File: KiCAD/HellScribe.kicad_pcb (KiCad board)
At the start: 2 copper layers, 173.7 x 28.4 mm, 49 parts, among them CON1 +12v, J1 STX-3100-5N, Q1 2N3904, Q10 2N3904, Q2 Q_PMOS_GSD, Q3 Q_PMOS_GSD, Q4 Q_PMOS_GSD, Q5 Q_PMOS_GSD, Q6 Q_PMOS_GSD, Q7 Q_PMOS_GSD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

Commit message: Improved PS filtering, updated version to v1.1
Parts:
- added C7: 10uF, Resistors_SMD:R_1206_HandSoldering, F.Cu at (54.4, 115.6)
- added L1: 10uH, Resistors_SMD:R_0805_HandSoldering, F.Cu at (55.1, 118.4)
- moved C6 1.02 mm to (50.8, 119.4)
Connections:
- C6 pad 2: +12V -> Net-(C6-Pad2)
- CON1 pad 1: +12V -> Net-(C6-Pad2)
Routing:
- net Net-(C6-Pad2): track 0.00 -> 6.82 mm
- net +12V: track 36.9 -> 32.7 mm, vias 14 -> 15
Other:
- board text added: "HellScribe v1.1"
- board text removed: "HellScribe v1.0"
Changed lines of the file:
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@@
 (kicad_pcb (version 4) (host pcbnew 4.0.2-stable)
   (general
-    (links 90)
+    (links 93)
     (no_connects 0)
-    (area 31.75 96.52 208.280001 128.270001)
+    (area 32.944999 97.968999 206.831001 126.567001)
     (thickness 1.6)
     (drawings 9)
-    (tracks 350)
+    (tracks 355)
     (zones 0)
-    (modules 49)
-    (nets 41)
+    (modules 51)
+    (nets 42)
   )
   (page A4)
@@
   )
   (setup
-    (last_trace_width 0.25)
+    (last_trace_width 0.5)
     (user_trace_width 0.5)
     (trace_clearance 0.2)
@@
   (net 39 "Net-(U2-Pad12)")
   (net 40 "Net-(Q1-Pad3)")
+  (net 41 "Net-(C6-Pad2)")
   (net_class Default "This is the default net class."
     (clearance 0.2)
@@
     (add_net "Net-(C4-Pad2)")
     (add_net "Net-(C5-Pad2)")
+    (add_net "Net-(C6-Pad2)")
     (add_net "Net-(D1-Pad1)")
     (add_net "Net-(D1-Pad2)")
@@
   )
   (module Capacitors_SMD:C_0603_HandSoldering (layer F.Cu)
-    (at 51.816 119.38 90)
+    (at 50.8 119.38 90)
     (descr "Capacitor SMD 0603, hand soldering")
     (tags "capacitor 0603")
     (attr smd)
-    (fp_text reference C6 (at 0 1.778 90) (layer F.SilkS)
+    (fp_text reference C6 (at -3.048 0 90) (layer F.SilkS)
       (effects (font (size 1 1) (thickness 0.15)))
     )
@@
       (net 2 GND))
     (pad 2 smd rect (at 0.95 0 90) (size 1.2 0.75) (layers F.Cu F.Paste F.Mask)
-      (net 8 +12V))
+      (net 41 "Net-(C6-Pad2)"))
     (model Capacitors_SMD.3dshapes/C_0603_HandSoldering.wrl
       (at (xyz 0 0 0))
@@
     (fp_line (start 7.00024 -4.50088) (end -7.50062 -4.50088) (layer F.SilkS) (width 0.15))
     (pad 1 thru_hole rect (at 6.20014 0) (size 3.50012 3.50012) (drill oval 1.00076 2.99974) (layers *.Cu *.Mask F.SilkS)
-      (net 8 +12V))
+      (net 41 "Net-(C6-Pad2)"))
     (pad 2 thru_hole rect (at 0.20066 0) (size 3.50012 3.50012) (drill oval 1.00076 2.99974) (layers *.Cu *.Mask F.SilkS)
       (net 2 GND))
@@
     )
   )
-  (gr_text "HellScribe v1.0" (at 171.704 104.14) (layer F.SilkS)
+  (module Resistors_SMD:R_1206_HandSoldering (layer F.Cu)
+    (at 54.356 115.57)
+    (descr "Resistor SMD 1206, hand soldering")
+    (tags "resistor 1206")
+    (attr smd)
+    (fp_text reference C7 (at -4.572 0) (layer F.SilkS)
+      (effects (font (size 1 1) (thickness 0.15)))
+    )
+    (fp_text value 10uF (at 0 2.3) (layer F.Fab)
+      (effects (font (size 1 1) (thickness 0.15)))
+    )
+    (fp_line (start -3.3 -1.2) (end 3.3 -1.2) (layer F.CrtYd) (width 0.05))
+    (fp_line (start -3.3 1.2) (end 3.3 1.2) (layer F.CrtYd) (width 0.05))
+    (fp_line (start -3.3 -1.2) (end -3.3 1.2) (layer F.CrtYd) (width 0.05))
+    (fp_line (start 3.3 -1.2) (end 3.3 1.2) (layer F.CrtYd) (width 0.05))
+    (fp_line (start 1 1.075) (end -1 1.075) (layer F.SilkS) (width 0.15))
+    (fp_line (start -1 -1.075) (end 1 -1.075) (layer F.SilkS) (width 0.15))
+    (pad 1 smd rect (at -2 0) (size 2 1.7) (layers F.Cu F.Paste F.Mask)
+      (net 2 GND))
+    (pad 2 smd rect (at 2 0) (size 2 1.7) (layers F.Cu F.Paste F.Mask)
+      (net 8 +12V))
+    (model Resistors_SMD.3dshapes/R_1206_HandSoldering.wrl
+      (at (xyz 0 0 0))
+      (scale (xyz 1 1 1))
+      (rotate (xyz 0 0 0))
+    )
+  )
+  (module Resistors_SMD:R_0805_HandSoldering (layer F.Cu)
+    (at 55.118 118.364 180)
+    (descr "Resistor SMD 0805, hand soldering")
+    (tags "resistor 0805")
+    (attr smd)
+    (fp_text reference L1 (at 0 -2.032 180) (layer F.SilkS)
+      (effects (font (size 1 1) (thickness 0.15)))
+    )
+    (fp_text value 10uH (at 0 2.1 180) (layer F.Fab)
+      (effects (font (size 1 1) (thickness 0.15)))
+    )
+    (fp_line (start -2.4 -1) (end 2.4 -1) (layer F.CrtYd) (width 0.05))
+    (fp_line (start -2.4 1) (end 2.4 1) (layer F.CrtYd) (width 0.05))
+    (fp_line (start -2.4 -1) (end -2.4 1) (layer F.CrtYd) (width 0.05))
+    (fp_line (start 2.4 -1) (end 2.4 1) (layer F.CrtYd) (width 0.05))
+    (fp_line (start 0.6 0.875) (end -0.6 0.875) (layer F.SilkS) (width 0.15))
+    (fp_line (start -0.6 -0.875) (end 0.6 -0.875) (layer F.SilkS) (width 0.15))
+    (pad 1 smd rect (at -1.35 0 180) (size 1.5 1.3) (layers F.Cu F.Paste F.Mask)
+      (net 8 +12V))
+    (pad 2 smd rect (at 1.35 0 180) (size 1.5 1.3) (layers F.Cu F.Paste F.Mask)
+      (net 41 "Net-(C6-Pad2)"))
+    (model Resistors_SMD.3dshapes/R_0805_HandSoldering.wrl
+      (at (xyz 0 0 0))
+      (scale (xyz 1 1 1))
+      (rotate (xyz 0 0 0))
+    )
+  )
+  (gr_text "HellScribe v1.1" (at 171.704 104.14) (layer F.SilkS)
     (effects (font (size 3 3) (thickness 0.5)))
   )
@@
   (segment (start 64.45 103.528) (end 64.6 103.378) (width 0.25) (layer F.Cu) (net 7))
   (segment (start 64.346 105.56) (end 64.45 105.664) (width 0.25) (layer F.Cu) (net 7))
-  (segment (start 51.816 118.43) (end 54.61 118.43) (width 0.5) (layer F.Cu) (net 8))
-  (segment (start 56.558 119.042) (end 55.946 118.43) (width 0.5) (layer F.Cu) (net 8))
-  (segment (start 55.946 118.43) (end 54.61 118.43) (width 0.5) (layer F.Cu) (net 8))
-  (segment (start 56.558 119.042) (end 56.558 122.682) (width 0.5) (layer F.Cu) (net 8))
-  (segment (start 51.816 118.43) (end 47.16014 118.43) (width 0.5) (layer F.Cu) (net 8))
-  (segment (start 47.16014 118.43) (end 47.09414 118.364) (width 0.5) (layer F.Cu) (net 8))
+  (segment (start 56.558 122.682) (end 54.61 122.682) (width 0.5) (layer F.Cu) (net 8))
+  (via (at 54.61 122.682) (size 0.6) (drill 0.4) (layers F.Cu B.Cu) (net 8))
+  (segment (start 56.468 118.364) (end 56.468 122.592) (width 0.5) (layer F.Cu) (net 8))
+  (segment (start 56.468 122.592) (end 56.558 122.682) (width 0.5) (layer F.Cu) (net 8))
+  (segment (start 56.468 118.364) (end 56.468 115.682) (width 0.5) (layer F.Cu) (net 8))
+  (segment (start 56.468 115.682) (end 56.356 115.57) (width 0.5) (layer F.Cu) (net 8))
   (segment (start 55.626 105.58) (end 55.626 103.886) (width 0.5) (layer F.Cu) (net 8))
   (via (at 55.626 103.886) (size 0.6) (drill 0.4) (layers F.Cu B.Cu) (net 8))
@@
   (segment (start 59.055 108.077) (end 58.674 108.458) (width 0.25) (layer F.Cu) (net 40))
   (segment (start 58.758 122.258) (end 58.758 122.682) (width 0.25) (layer F.Cu) (net 40))
+  (segment (start 50.8 118.43) (end 53.702 118.43) (width 0.5) (layer F.Cu) (net 41))
+  (segment (start 53.702 118.43) (end 53.768 118.364) (width 0.5) (layer F.Cu) (net 41))
+  (segment (start 47.09414 118.364) (end 50.734 118.364) (width 0.5) (layer F.Cu) (net 41))
+  (segment (start 50.734 118.364) (end 50.8 118.43) (width 0.5) (layer F.Cu) (net 41))
+  (segment (start 47.16014 118.43) (end 47.09414 118.364) (width 0.5) (layer F.Cu) (net 41))
   (zone (net 2) (net_name GND) (layer F.Cu) (hatch edge 0.508)
     (connect_pads (clearance 0.254))

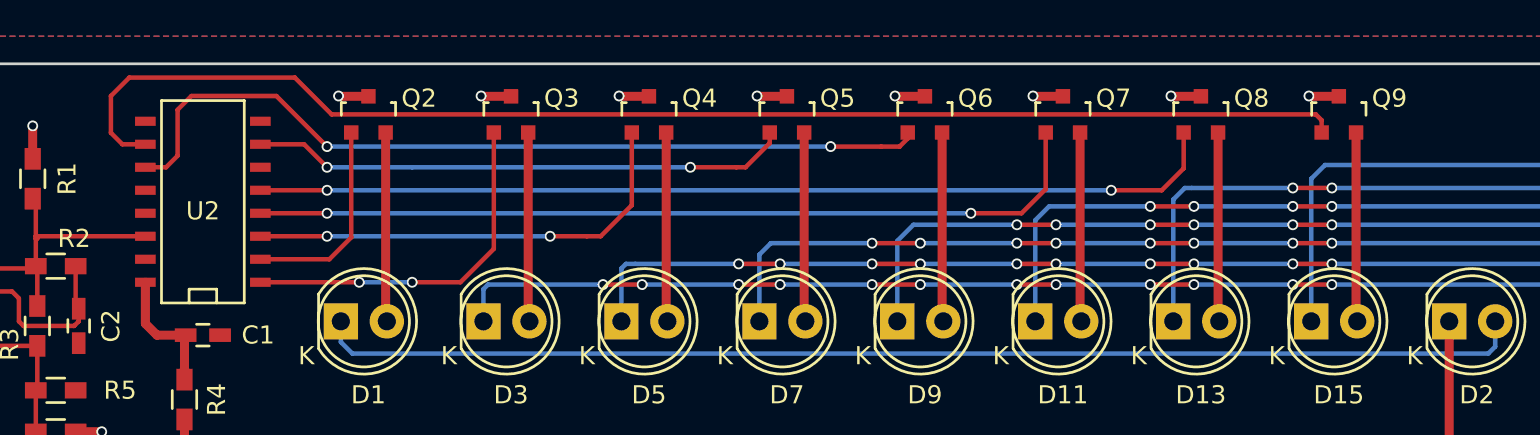
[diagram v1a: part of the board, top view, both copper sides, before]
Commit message: Fixed PMOS orientation.
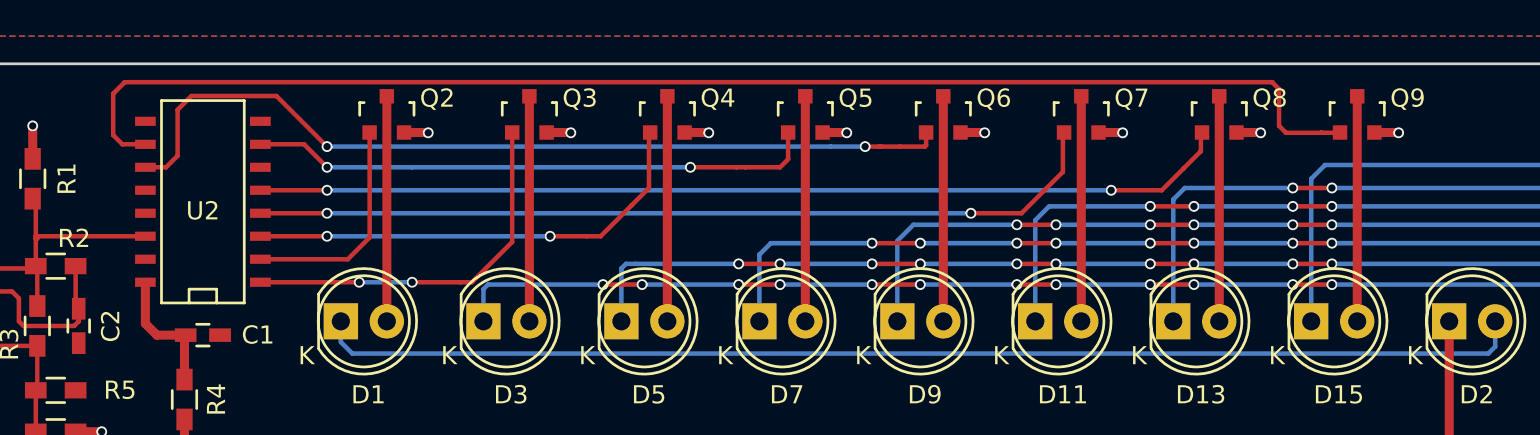
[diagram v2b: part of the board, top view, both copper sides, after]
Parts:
- Q2, Q3, Q4, Q5, Q6, Q7, Q8, Q9: value Q_PMOS_GSD -> FDV304P
- moved Q9 1.02 mm to (142.2, 100.8)
- moved Q2 1.02 mm to (88.6, 100.8)
- moved Q4 1.02 mm to (104.1, 100.8)
- moved Q5 1.02 mm to (111.8, 100.8)
- moved Q7 1.02 mm to (127.0, 100.8)
- moved Q3 1.02 mm to (96.5, 100.8)
- moved Q6 1.02 mm to (119.4, 100.8)
- moved Q8 1.02 mm to (134.6, 100.8)
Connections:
- Q2 pad 2: Net-(D1-Pad2) -> +12V
- Q2 pad 3: +12V -> Net-(D1-Pad2)
- Q3 pad 2: Net-(D3-Pad2) -> +12V
- Q3 pad 3: +12V -> Net-(D3-Pad2)
- Q4 pad 2: Net-(D5-Pad2) -> +12V
- Q4 pad 3: +12V -> Net-(D5-Pad2)
- Q5 pad 2: Net-(D7-Pad2) -> +12V
- Q5 pad 3: +12V -> Net-(D7-Pad2)
- Q6 pad 2: Net-(D9-Pad2) -> +12V
- Q6 pad 3: +12V -> Net-(D9-Pad2)
- Q7 pad 2: Net-(D11-Pad2) -> +12V
- Q7 pad 3: +12V -> Net-(D11-Pad2)
- Q8 pad 2: Net-(D13-Pad2) -> +12V
- Q8 pad 3: +12V -> Net-(D13-Pad2)
- Q9 pad 2: Net-(D15-Pad2) -> +12V
- Q9 pad 3: +12V -> Net-(D15-Pad2)
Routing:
- net +12V: track 32.7 -> 30.2 mm
- net Net-(D15-Pad2): track 10.2 -> 12.5 mm
- net Net-(D13-Pad2): track 10.2 -> 12.5 mm
- net Net-(D9-Pad2): track 10.5 -> 12.5 mm
- net Net-(D7-Pad2): track 10.5 -> 12.5 mm
- net Net-(D5-Pad2): track 10.5 -> 12.5 mm
- net Net-(D11-Pad2): track 10.5 -> 12.5 mm
- net Net-(D1-Pad2): track 10.5 -> 12.4 mm
- net Net-(D3-Pad2): track 10.5 -> 12.4 mm
- net Net-(Q5-Pad1): track 29.8 -> 31.3 mm
- net Net-(Q9-Pad1): track 73.1 -> 74.7 mm
- net Net-(Q6-Pad1): track 46.9 -> 48.3 mm
- net Net-(Q2-Pad1): track 11.3 -> 12.3 mm
- net Net-(Q3-Pad1): track 20.1 -> 20.9 mm
